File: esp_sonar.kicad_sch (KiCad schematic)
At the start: 9 parts, among them U1 TL072

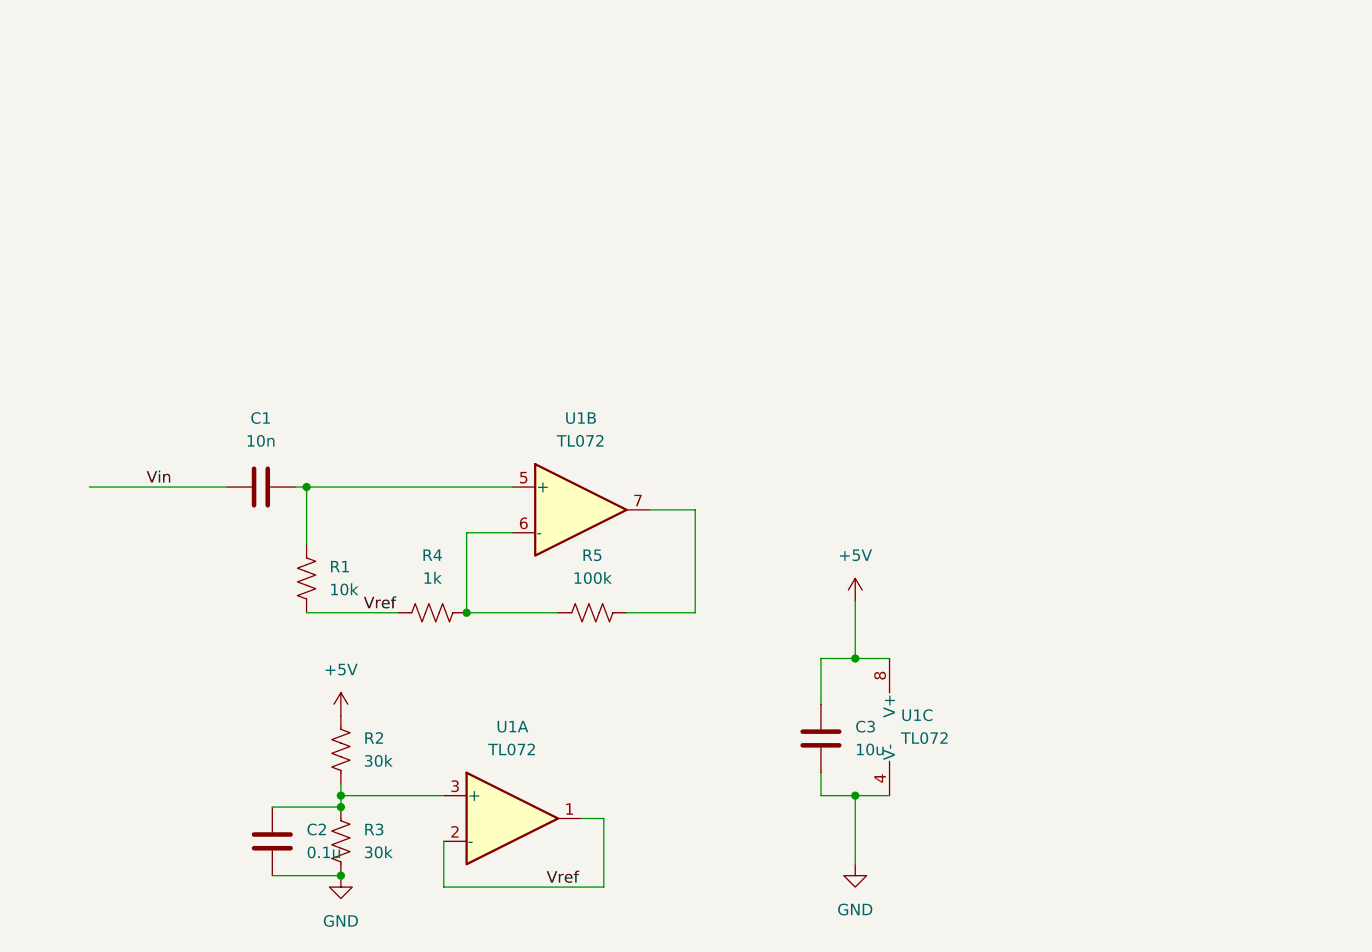
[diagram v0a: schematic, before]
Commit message: Input amplification works, output in progress
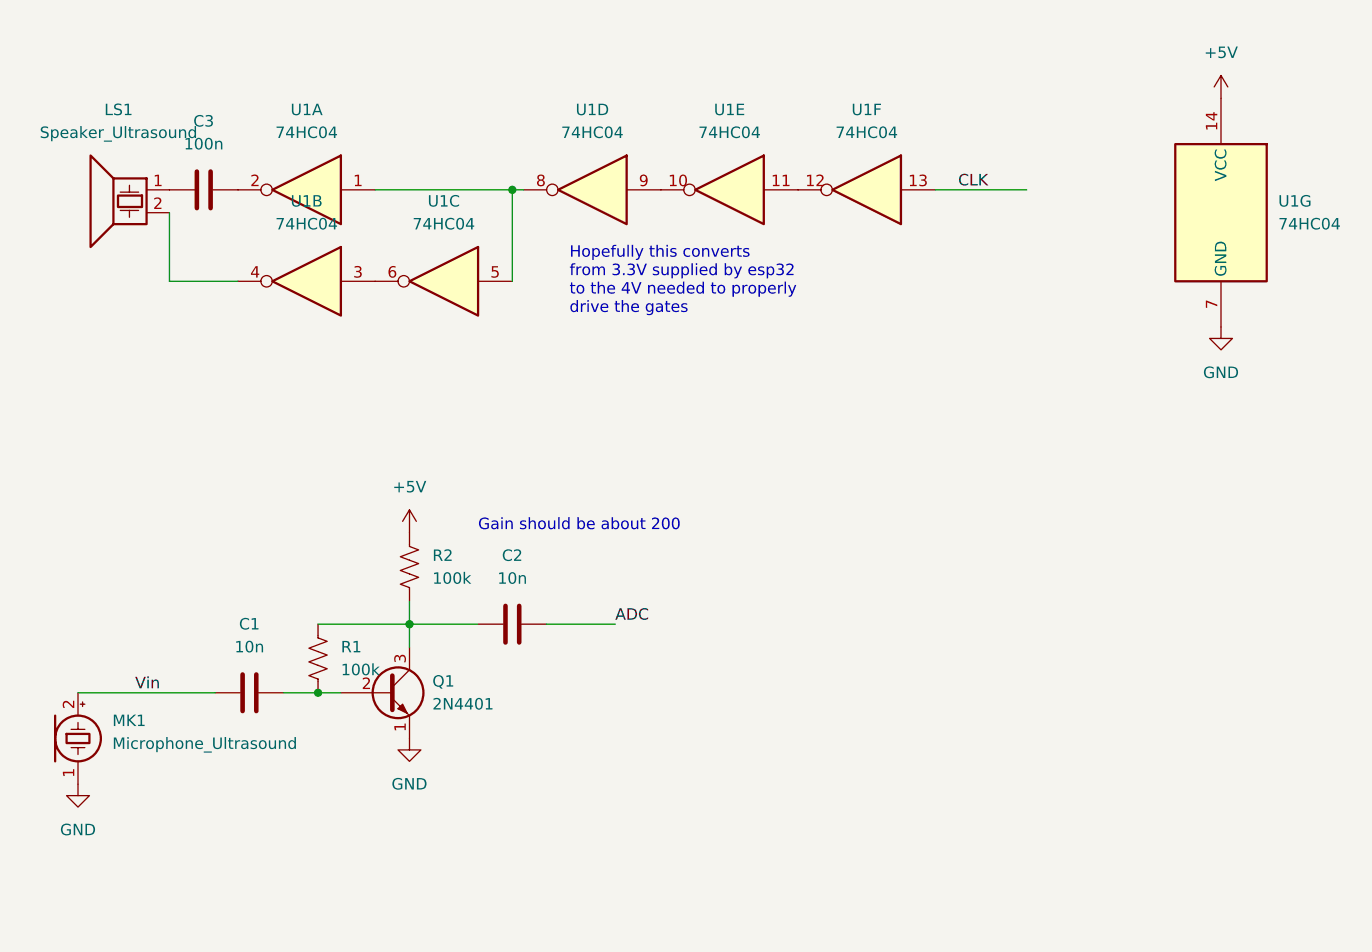
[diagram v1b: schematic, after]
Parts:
- removed R3: 30k, Resistor_THT:R_Axial_DIN0207_L6.3mm_D2.5mm_P2.54mm_Vertical, symbol Device:R_US
- removed R4: 1k, Resistor_THT:R_Axial_DIN0207_L6.3mm_D2.5mm_P2.54mm_Vertical, symbol Device:R_US
- removed R5: 100k, Resistor_THT:R_Axial_DIN0207_L6.3mm_D2.5mm_P2.54mm_Vertical, symbol Device:R_US
- removed U1: TL072, Package_DIP:DIP-8_W7.62mm, symbol Amplifier_Operational:TL072
- added LS1: Speaker_Ultrasound, Connector_PinHeader_2.54mm:PinHeader_1x02_P2.54mm_Vertical, symbol Device:Speaker_Ultrasound
- added MK1: Microphone_Ultrasound, Connector_PinHeader_2.54mm:PinHeader_1x02_P2.54mm_Vertical, symbol Device:Microphone_Ultrasound
- added Q1: 2N4401, Package_TO_SOT_THT:TO-92_Inline, symbol kamocat:2N4401
- added U1: 74HC04, Package_DIP:DIP-14_W7.62mm_Socket, symbol 74xx:74HC04
- C2: value 0.1u -> 10n
- C3: value 10u -> 100n
- R1: value 10k -> 100k; footprint Resistor_THT:R_Axial_DIN0207_L6.3mm_D2.5mm_P2.54mm_Vertical -> Resistor_THT:R_Axial_DIN0207_L6.3mm_D2.5mm_P10.16mm_Horizontal
- R2: value 30k -> 100k; footprint Resistor_THT:R_Axial_DIN0207_L6.3mm_D2.5mm_P2.54mm_Vertical -> Resistor_THT:R_Axial_DIN0207_L6.3mm_D2.5mm_P10.16mm_Horizontal
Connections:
- net Vref is gone; now on an unnamed net: R1.2
- net +5V: now also U1.14 (VCC); no longer C3.1
- net GND: now also MK1.1 (-), Q1.1 (E), U1.7 (GND); no longer C2.2, C3.2
- net Vin: now also MK1.2 (+)
- net at C2.1, R2.2: now also R1.1, Q1.3 (C)
- net at C1.2: now also Q1.2 (B); no longer R1.1
- new net: U1.11, U1.12
- new net: U1.3, U1.6
- new net: LS1.2, U1.4
- new net: C3.1, LS1.1
- new net: C3.2, U1.2
- new net: U1.1, U1.5, U1.8
- new net: U1.10, U1.9
- new net ADC: C2.2
- new net CLK: U1.13
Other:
- note added: "Gain should be about 200"
- note added: "Hopefully this converts from 3.3V supplied by esp32 to the 4V needed to properly drive the gates"
- moved on the sheet: C1

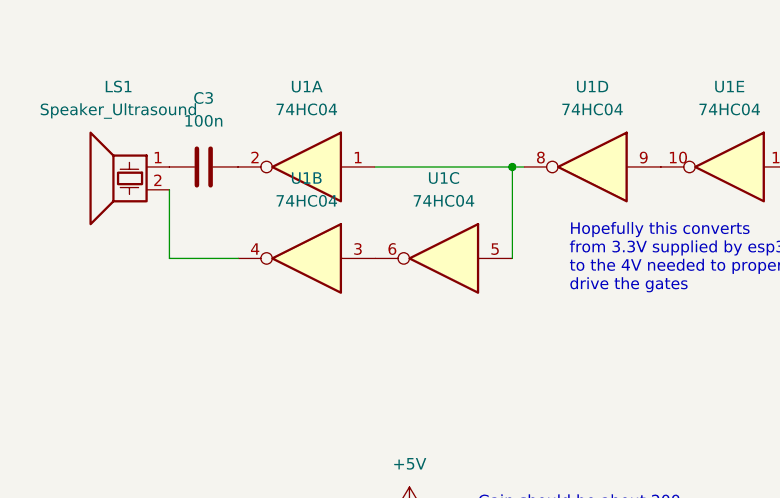
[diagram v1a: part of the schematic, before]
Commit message: Output driver works, but is overkill
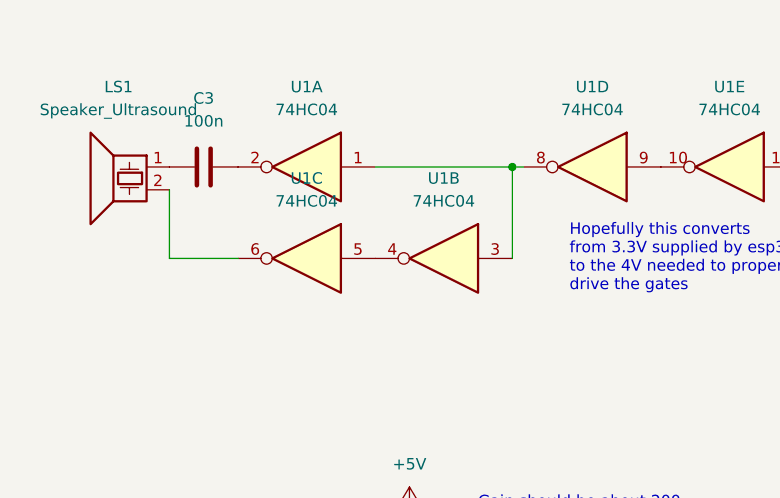
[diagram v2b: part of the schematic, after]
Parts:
- C1, C2, C3: footprint Capacitor_THT:C_Disc_D3.4mm_W2.1mm_P2.50mm -> Capacitor_THT:C_Disc_D4.7mm_W2.5mm_P5.00mm
- Q1: footprint Package_TO_SOT_THT:TO-92_Inline -> Package_TO_SOT_THT:TO-92_Inline_Wide
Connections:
- net at U1.3: now also U1.1, U1.8; no longer U1.6
- net at U1.4: now also U1.5; no longer LS1.2
- new net: LS1.2, U1.6
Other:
- moved on the sheet: U1B, U1C

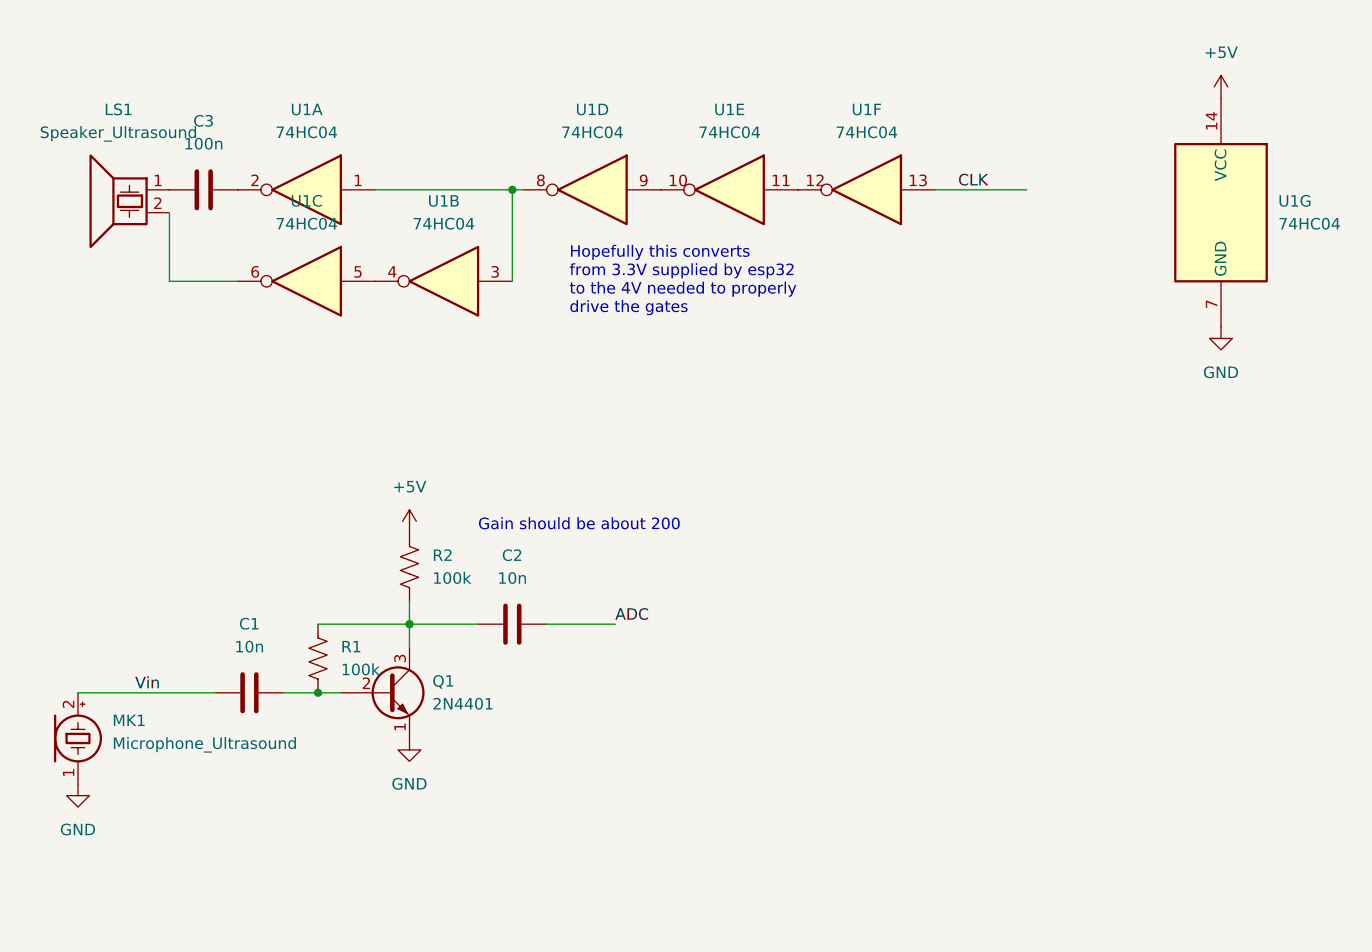
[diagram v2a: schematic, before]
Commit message: Protoboard layout
Simplified driver to single-stage mosfet inverter
Keeping the speakers off-board to maintain form factor
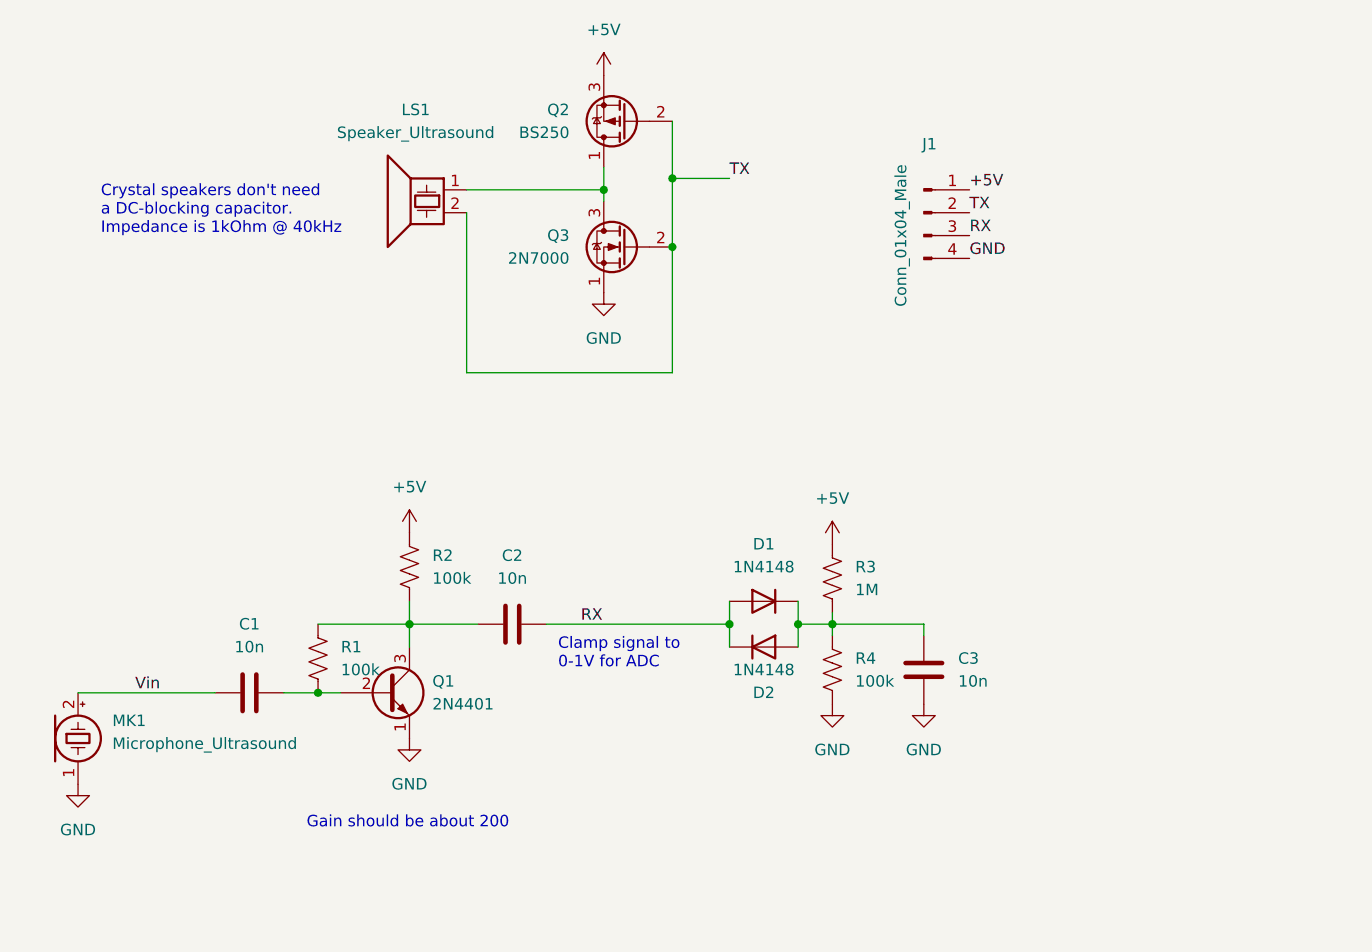
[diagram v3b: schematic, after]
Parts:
- removed U1: 74HC04, Package_DIP:DIP-14_W7.62mm_Socket, symbol 74xx:74HC04
- added D1, D2: 1N4148, Diode_THT:D_DO-35_SOD27_P7.62mm_Horizontal, symbol Diode:1N4148
- added J1: Conn_01x04_Male, Connector_PinHeader_2.54mm:PinHeader_1x04_P2.54mm_Horizontal, symbol Connector:Conn_01x04_Male
- added Q2: BS250, Package_TO_SOT_THT:TO-92_Inline, symbol Transistor_FET:BS250
- added Q3: 2N7000, Package_TO_SOT_THT:TO-92_Inline, symbol Transistor_FET:2N7000
- added R3: 1M, Resistor_THT:R_Axial_DIN0207_L6.3mm_D2.5mm_P10.16mm_Horizontal, symbol Device:R_US
- added R4: 100k, Resistor_THT:R_Axial_DIN0207_L6.3mm_D2.5mm_P10.16mm_Horizontal, symbol Device:R_US
- C3: value 100n -> 10n
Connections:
- net +5V: now also J1.1 (Pin_1), Q2.3 (S), R3.1
- net GND: now also C3.2, J1.4 (Pin_4), Q3.1 (S), R4.2
- net at C3.1: now also D1.1 (K), D2.2 (A), R3.2, R4.1; no longer LS1.1
- net TX: now reaches LS1.2
- net TX: now also J1.2 (Pin_2), Q2.2 (G), Q3.2 (G)
- net ADC renamed RX
- net RX: now also D1.2 (A), D2.1 (K), J1.3 (Pin_3)
- new net: LS1.1, Q2.1 (D), Q3.3 (D)
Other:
- note added: "Clamp signal to 0-1V for ADC"
- note added: "Crystal speakers don't need a DC-blocking capacitor. Impedance is 1kOhm @ 40kHz"
- note removed: "Hopefully this converts from 3.3V supplied by esp32 to the 4V needed to properly drive the gates"
- moved on the sheet: LS1

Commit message: Improved layout
Added R5 to prevent shoot-through when dle
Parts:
- added R5: 100k, Resistor_THT:R_Axial_DIN0207_L6.3mm_D2.5mm_P2.54mm_Vertical, symbol Device:R_US
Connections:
- net GND: now also R5.2
- net TX: now also R5.1
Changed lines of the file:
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@@
   (junction (at 93.98 66.04) (diameter 0) (color 0 0 0 0)
   )
+  (junction (at 107.95 64.77) (diameter 0) (color 0 0 0 0)
+  )
   (junction (at 119.38 114.3) (diameter 0) (color 0 0 0 0)
   )
@@
   (junction (at 107.95 114.3) (diameter 0) (color 0 0 0 0)
   )
+  (wire (pts (xy 107.95 64.77) (xy 111.76 64.77))
+    (stroke (width 0) (type default) (color 0 0 0 0))
+  )
   (wire (pts (xy 115.57 111.76) (xy 115.57 114.3))
     (stroke (width 0) (type default) (color 0 0 0 0))
@@
     (stroke (width 0) (type default) (color 0 0 0 0))
   )
+  (wire (pts (xy 107.95 64.77) (xy 107.95 71.12))
+    (stroke (width 0) (type default) (color 0 0 0 0))
+  )
   (wire (pts (xy 107.95 111.76) (xy 107.95 114.3))
     (stroke (width 0) (type default) (color 0 0 0 0))
@@
     (stroke (width 0) (type default) (color 0 0 0 0))
   )
-  (wire (pts (xy 107.95 64.77) (xy 101.6 64.77))
+  (wire (pts (xy 101.6 64.77) (xy 107.95 64.77))
     (stroke (width 0) (type default) (color 0 0 0 0))
   )
@@
     (effects (font (size 1.27 1.27)) (justify left bottom))
   )
-  (label "TX" (at 107.95 64.77 0)
+  (label "TX" (at 111.76 64.77 0)
     (effects (font (size 1.27 1.27)) (justify left bottom))
   )
@@
     (pin "2")
   )
+  (symbol (lib_id "power:GND") (at 107.95 78.74 0) (unit 1)
+    (in_bom yes) (on_board yes) (fields_autoplaced)
+    (property "Reference" "#PWR08" (id 0) (at 107.95 85.09 0)
+      (effects (font (size 1.27 1.27)) hide)
+    )
+    (property "Value" "GND" (id 1) (at 107.95 83.82 0))
+    (property "Footprint" "" (id 2) (at 107.95 78.74 0)
+      (effects (font (size 1.27 1.27)) hide)
+    )
+    (property "Datasheet" "" (id 3) (at 107.95 78.74 0)
+      (effects (font (size 1.27 1.27)) hide)
+    )
+    (pin "1")
+  )
+  (symbol (lib_id "Device:R_US") (at 107.95 74.93 0) (unit 1)
+    (in_bom yes) (on_board yes) (fields_autoplaced)
+    (property "Reference" "R5" (id 0) (at 110.49 73.6599 0)
+      (effects (font (size 1.27 1.27)) (justify left))
+    )
+    (property "Value" "100k" (id 1) (at 110.49 76.1999 0)
+      (effects (font (size 1.27 1.27)) (justify left))
+    )
+    (property "Footprint" "Resistor_THT:R_Axial_DIN0207_L6.3mm_D2.5mm_P2.54mm_Vertical" (id 2) (at 108.966 75.184 90)
+      (effects (font (size 1.27 1.27)) hide)
+    )
+    (property "Datasheet" "~" (id 3) (at 107.95 74.93 0)
+      (effects (font (size 1.27 1.27)) hide)
+    )
+    (pin "1")
+    (pin "2")
+  )
   (symbol (lib_id "Device:R_US") (at 119.38 119.38 0) (unit 1)
     (in_bom yes) (on_board yes) (fields_autoplaced)
@@
       (reference "#PWR07") (unit 1) (value "GND") (footprint "")
     )
+    (path "/46c62521-3389-4214-8f35-9a2436fc56ac"
+      (reference "#PWR08") (unit 1) (value "GND") (footprint "")
+    )
     (path "/2c59491a-3564-4661-a789-5350cc5b0011"
       (reference "#PWR0101") (unit 1) (value "GND") (footprint "")
@@
       (reference "R4") (unit 1) (value "100k") (footprint "Resistor_THT:R_Axial_DIN0207_L6.3mm_D2.5mm_P10.16mm_Horizontal")
     )
-  )
+    (path "/5b0b81f7-99d8-4b9e-8bf6-3f4b56a1f4f0"
+      (reference "R5") (unit 1) (value "100k") (footprint "Resistor_THT:R_Axial_DIN0207_L6.3mm_D2.5mm_P2.54mm_Vertical")
+    )
+  )
